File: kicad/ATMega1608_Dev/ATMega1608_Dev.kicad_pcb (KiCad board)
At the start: 4 copper layers, 55.9 x 25.4 mm, 37 parts, among them J1 Alt Power, J101 GPIO2, J2 USB_B_Micro, J3 Comm, J4 GPIO1, J6 Power OUT, U1 TC1262-33, U2 FT232RQ, U3 ATMega1608_32

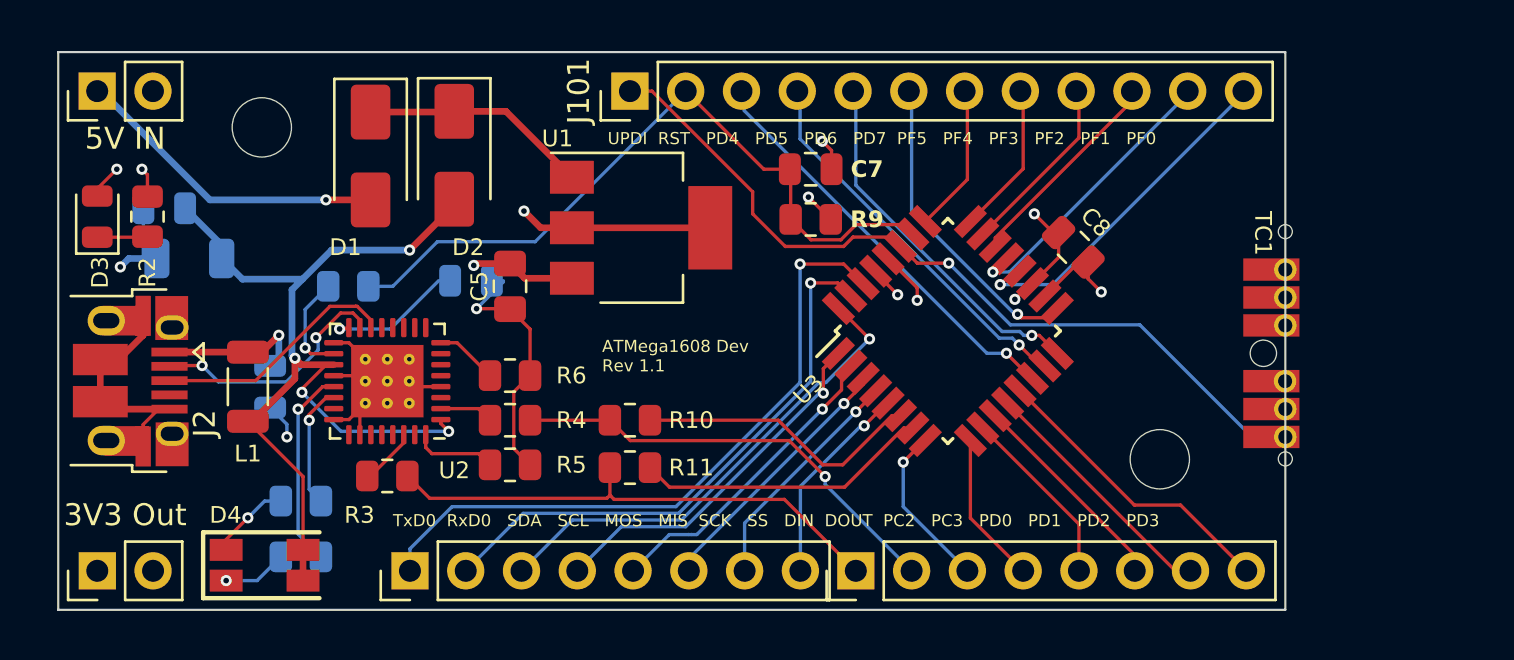
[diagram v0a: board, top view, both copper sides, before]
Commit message: Removes the FT232 and replaces with a UM2102N port
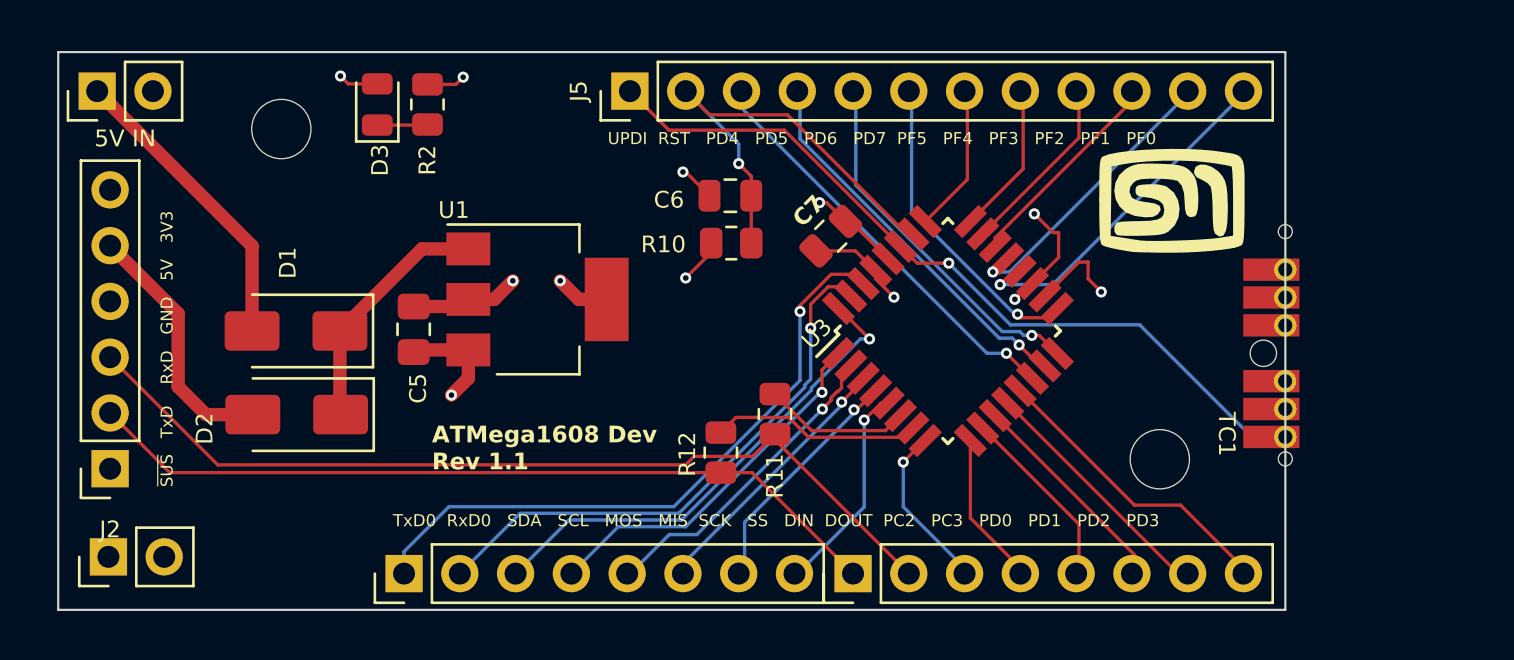
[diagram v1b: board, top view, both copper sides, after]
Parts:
- removed C1: 10nF, Capacitor_SMD:C_0805_2012Metric
- removed C2, C4, C8: 100nF, Capacitor_SMD:C_0805_2012Metric
- removed C3: 4.7μF, Capacitor_SMD:C_1206_3216Metric
- removed D4: RED_GREEN, atmega1608_footprints:LED_KKAA_15-22SURSYGC
- removed J101: GPIO2, Connector_PinHeader_2.54mm:PinHeader_1x12_P2.54mm_Vertical
- removed L1: 33Ω, Inductor_SMD:L_1206_3216Metric
- removed LG3: logo, Symbol:KiCad-Logo_5mm_SilkScreen
- removed R1, R3, R4: 0Ω, Resistor_SMD:R_0805_2012Metric
- removed R5, R6: NOPOP, Resistor_SMD:R_0805_2012Metric
- removed R7, R8: 270Ω, Resistor_SMD:R_0805_2012Metric
- removed R9: 10kΩ, Resistor_SMD:R_0805_2012Metric
- removed U2: FT232RQ, Package_DFN_QFN:QFN-32-1EP_5x5mm_P0.5mm_EP3.3x3.3mm_ThermalVias
- added C6: 100nF, Capacitor_SMD:C_0805_2012Metric, F.Cu at (142.4, 56.8)
- added J5: GPIO2, Connector_PinHeader_2.54mm:PinHeader_1x12_P2.54mm_Vertical, F.Cu at (137.8, 52.1)
- added LG2: logo, Symbol:KiCad-Logo_5mm_SilkScreen, B.Cu at (157.9, 59.6)
- added R12: 0Ω, Resistor_SMD:R_0805_2012Metric, F.Cu at (141.9, 68.5)
- J2: value USB_B_Micro -> USART-USB; footprint atmega1608_footprints:USB_Micro-B_Amphenol_10103594-0001LF_Horizontal -> Connector_PinSocket_2.54mm:PinSocket_1x06_P2.54mm_Vertical
- J3: value Comm -> GPIO1
- J4: value GPIO1 -> Power OUT; footprint Connector_PinHeader_2.54mm:PinHeader_1x08_P2.54mm_Vertical -> Connector_PinHeader_2.54mm:PinHeader_1x02_P2.54mm_Vertical
- J6: value Power OUT -> Comm; footprint Connector_PinHeader_2.54mm:PinHeader_1x02_P2.54mm_Vertical -> Connector_PinHeader_2.54mm:PinHeader_1x08_P2.54mm_Vertical
- LG1: moved to F.Cu
- R10: value 0Ω -> 10kΩ
- moved J4 34.0 mm to (114.0, 73.3)
- moved J3 20.2 mm to (148.0, 74.0)
- moved J6 14.0 mm to (127.5, 74.0)
- moved D2 13.8 mm to (122.6, 66.8), turned to 180 degrees
- moved R2 13.7 mm to (128.6, 52.7)
- moved D3 13.7 mm to (126.3, 52.7)
- moved R10 9.29 mm to (142.4, 59.0)
- moved D1 8.66 mm to (122.6, 63.0), turned to 180 degrees
- moved R11 7.04 mm to (144.4, 66.8), turned to -90 degrees
- moved U1 5.74 mm to (133.6, 61.6)
- moved C5 4.80 mm to (127.9, 62.9), turned to 90 degrees
- moved J2 4.10 mm to (114.1, 69.3), turned to 180 degrees
- moved C7 3.18 mm to (146.9, 58.7), turned to -135 degrees
- moved LG1 1.25 mm to (162.4, 57.0), turned to 0 degrees
- moved H2 0.89 mm to (121.9, 53.8)
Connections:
- C5 pad 1: +3V3 -> +3.3V
- C7 pad 1: /~{RESET} -> +3.3V
- D2 pad 2: Net-(D2-A) -> /USB-5V
- D3 pad 2: +3V3 -> +3.3V
- J2 pad 1: Net-(J2-VBUS) -> unconnected-(J2-Pin_1-Pad1)
- J2 pad 2: Net-(J2-D-) -> /DIN
- J2 pad 3: Net-(J2-D+) -> /DOUT
- J2 pad 4: unconnected-(J2-ID-Pad4) -> GND
- J2 pad 5: GND -> /USB-5V
- J2 pad 6: GND -> unconnected-(J2-Pin_6-Pad6)
- J3 pad 1: /TxD0 -> /DIN
- J3 pad 2: /RxD0 -> /DOUT
- J3 pad 3: /SDA -> /PC2
- J3 pad 4: /SCL -> /PC3
- J3 pad 5: /MOSI -> /PD0
- J3 pad 6: /MISO -> /PD1
- J3 pad 7: /SCK -> /PD2
- J3 pad 8: /SS -> /PD3
- J4 pad 1: /DIN -> +3.3V
- J4 pad 2: /DOUT -> GND
- J6 pad 1: +3V3 -> /TxD0
- J6 pad 2: GND -> /RxD0
- R10 pad 1: Net-(U3-PC0/TxD1/2-WO/1-IN0) -> /~{RESET}
- R10 pad 2: /DOUT -> +3.3V
- R11 pad 1: Net-(U3-PC1/RxD1-IN1) -> Net-(U3-PC0/TxD1/2-WO/1-IN0)
- R11 pad 2: /DIN -> /DOUT
- TC1 pad 2: +3V3 -> +3.3V
- U1 pad 3: +3V3 -> +3.3V
- U3 pad 18: +3V3 -> +3.3V
- U3 pad 19: unconnected-(U3-GND-Pad19) -> GND
- U3 pad 28: +3V3 -> +3.3V
- U3 pad 29: unconnected-(U3-GND-Pad29) -> GND
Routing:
- net Net-(D2-A): track 43.7 -> 0.00 mm, vias 4 -> 0
- net GND: track 52.6 -> 20.9 mm, vias 8 -> 7
- net /DOUT: track 20.4 -> 41.8 mm, vias 1 -> 0
- net +3.3V: track 0.00 -> 17.2 mm, vias 0 -> 5
- net +3V3: track 14.5 -> 0.00 mm, vias 5 -> 0
- net /DIN: track 23.6 -> 36.9 mm
- net /~{RESET}: track 33.1 -> 21.2 mm, vias 0 -> 1
- net /USB-5V: track 0.00 -> 11.6 mm
- net Net-(J2-D-): track 11.2 -> 0.00 mm, vias 2 -> 0
- net Net-(J2-D+): track 11.2 -> 0.00 mm
- net Net-(U2-CBUS1): track 9.21 -> 0.00 mm, vias 1 -> 0
- net Net-(J2-VBUS): track 6.86 -> 0.00 mm, vias 1 -> 0
- net Net-(U3-PC0/TxD1/2-WO/1-IN0): track 13.2 -> 6.69 mm
- net Net-(U2-3V3Out): track 5.83 -> 0.00 mm, vias 1 -> 0
- net Net-(U2-CBUS0): track 5.60 -> 0.00 mm, vias 1 -> 0
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- added copper zone on In2.Cu, net +3.3V
- removed copper zone on In2.Cu, net +3V3
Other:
- board text added: "~{SUS} TxD RxD GND 5V 3V3"

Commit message: Fixes label overflow
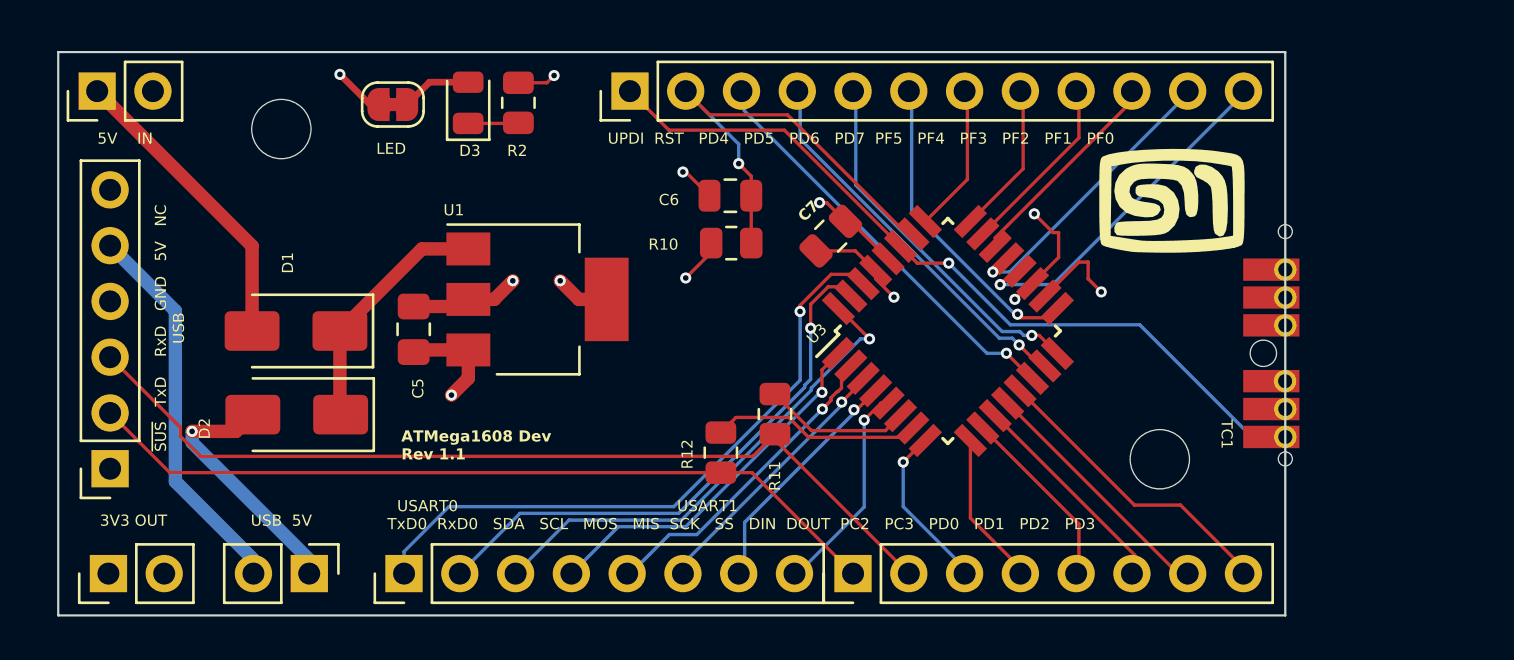
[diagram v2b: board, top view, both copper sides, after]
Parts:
- added JP101: USB Pwr, Connector_PinHeader_2.54mm:PinHeader_1x02_P2.54mm_Vertical, F.Cu at (123.2, 74.0)
- added JP102: Indicator LED, Jumper:SolderJumper-2_P1.3mm_Bridged_RoundedPad1.0x1.5mm, F.Cu at (127.0, 52.7)
- moved D3 4.14 mm to (130.4, 52.6)
- moved R2 4.14 mm to (132.7, 52.6)
- moved J4 0.76 mm to (114.0, 74.0)
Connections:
- D3 pad 2: +3.3V -> Net-(D3-A)
- J2 pad 5: /USB-5V -> Net-(J2-Pin_5)
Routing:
- net Net-(J2-Pin_5): track 0.00 -> 17.0 mm
- net Net-(D3-A): track 0.00 -> 3.20 mm
- net +3.3V: track 17.2 -> 17.7 mm
- net /USB-5V: track 11.6 -> 11.1 mm, vias 0 -> 1
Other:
- board size 55.9 x 25.4 mm -> 55.9 x 25.7 mm
- board text added: "LED"
- board text added: "USART0 USART1 TxD0 RxD0 SDA SCL MOS MIS SCK SS DIN DOUT PC2 PC3 PD0 PD1 PD2 PD3"
- board text added: "~{SUS} TxD RxD GND 5V NC USB"
- board text removed: "TxD0 RxD0 SDA SCL MOS MIS SCK SS DIN DOUT PC2 PC3 PD0 PD1 PD2 PD3"
- board text removed: "~{SUS} TxD RxD GND 5V 3V3"

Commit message: Revision 1.2 - Update to connectors, jumpers and labels
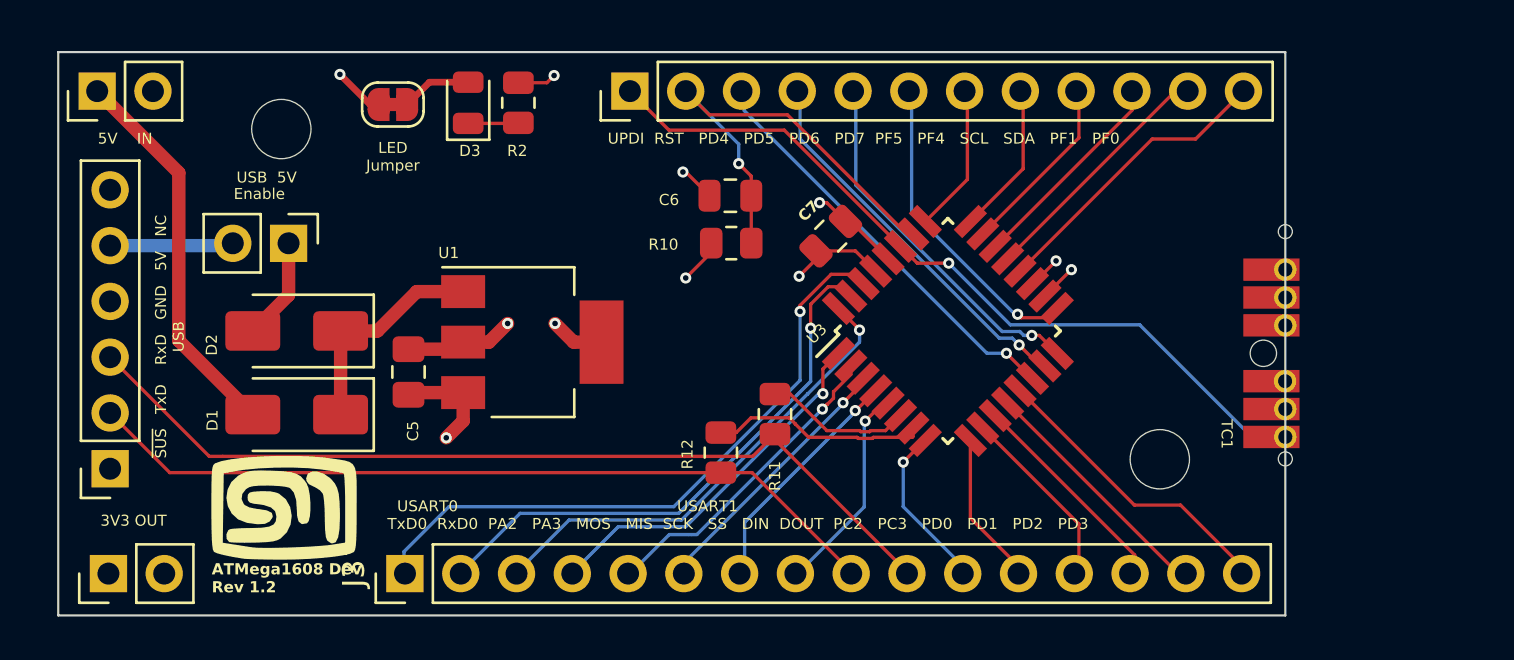
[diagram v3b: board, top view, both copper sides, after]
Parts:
- removed J6: Comm, Connector_PinHeader_2.54mm:PinHeader_1x08_P2.54mm_Vertical
- added LG3: logo, mech:MyBasic_rounded_50_1, B.Cu at (141.2, 59.8)
- J3: value GPIO1 -> GPIO; footprint Connector_PinHeader_2.54mm:PinHeader_1x08_P2.54mm_Vertical -> Connector_PinHeader_2.54mm:PinHeader_1x16_P2.54mm_Vertical
- moved LG1 42.8 mm to (122.0, 71.0)
- moved J3 20.4 mm to (127.5, 74.0)
- moved LG2 19.0 mm to (141.2, 68.8)
- moved JP101 15.1 mm to (122.2, 59.0)
- moved D1 3.81 mm to (122.6, 66.8)
- moved D2 3.81 mm to (122.6, 63.0)
- moved C5 1.96 mm to (127.7, 64.9)
- moved U1 1.96 mm to (133.3, 63.5)
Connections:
- J3 pad 1: /DIN -> /TxD0
- J3 pad 2: /DOUT -> /RxD0
- J3 pad 3: /PC2 -> /PA2
- J3 pad 4: /PC3 -> /PA3
- J3 pad 5: /PD0 -> /MOSI
- J3 pad 6: /PD1 -> /MISO
- J3 pad 7: /PD2 -> /SCK
- J3 pad 8: /PD3 -> /SS
- J5 pad 10: /PF2 -> /SDA
- J5 pad 9: /PF3 -> /SCL
- U3 pad 1: /SCL -> /PA3
- U3 pad 22: /PF2 -> /SDA
- U3 pad 23: /PF3 -> /SCL
- U3 pad 32: /SDA -> /PA2
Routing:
- net /PA2: track 0.00 -> 22.0 mm, vias 0 -> 1
- net /PA3: track 0.00 -> 17.0 mm, vias 0 -> 1
- net /SDA: track 22.6 -> 9.67 mm, vias 1 -> 0
- net Net-(J2-Pin_5): track 17.0 -> 5.63 mm
- net /PF2: track 9.70 -> 0.00 mm
- net /SCL: track 16.9 -> 8.32 mm, vias 1 -> 0
- net /PF3: track 8.32 -> 0.00 mm
- net /USB-5V: track 11.1 -> 4.67 mm, vias 1 -> 0
- net GND: track 20.9 -> 17.0 mm, vias 7 -> 6
- net Net-(D1-A): track 13.8 -> 17.7 mm
- net +3.3V: track 17.7 -> 15.2 mm
- net /PF0: track 16.0 -> 13.6 mm, vias 1 -> 0
- net /PF1: track 13.3 -> 11.4 mm, vias 1 -> 0
- net +5V: track 11.2 -> 10.1 mm
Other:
- board text added: "ATMega1608 Dev Rev 1.2"
- board text added: "Enable"
- board text added: "LED Jumper"
- board text added: "UPDI RST PD4 PD5 PD6 PD7 PF5 PF4 SCL SDA PF1 PF0"
- board text added: "USART0 USART1 TxD0 RxD0 PA2 PA3 MOS MIS SCK SS DIN DOUT PC2 PC3 PD0 PD1 PD2 PD3"
- board text removed: "ATMega1608 Dev Rev 1.1"
- board text removed: "LED"
- board text removed: "UPDI RST PD4 PD5 PD6 PD7 PF5 PF4 PF3 PF2 PF1 PF0"
- board text removed: "USART0 USART1 TxD0 RxD0 SDA SCL MOS MIS SCK SS DIN DOUT PC2 PC3 PD0 PD1 PD2 PD3"

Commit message: Adding a PCB release workflow
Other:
- board text added: "ATMega1608 Dev Rev ${RELEASE}"
